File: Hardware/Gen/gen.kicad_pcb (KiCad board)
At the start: 2 copper layers, 149.8 x 76.5 mm, 52 parts, among them J1 Screw_Terminal_01x03, J2 XLR4, J3 XLR3, J4 GAMEN, J5 SHORI, J6 MAE, J7 Screw_Terminal_01x02, J8 PJ-063BH, U1 TPS543021DRLR, U3 TPS560430YDBVR

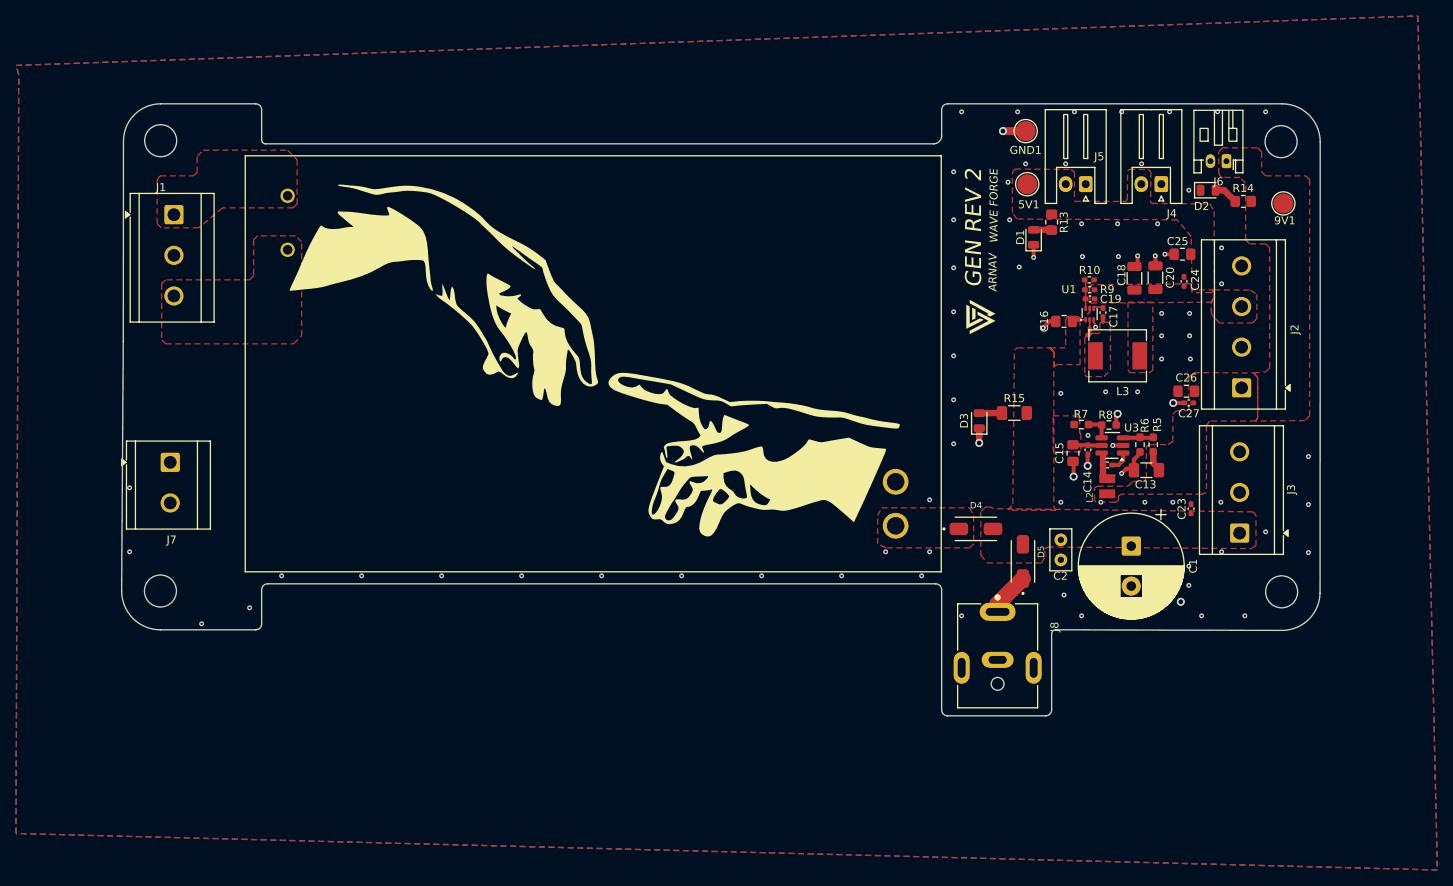
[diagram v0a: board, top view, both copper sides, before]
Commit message: Gen rev 2 Ordered and Assembled. Proven Working All rails Spot on
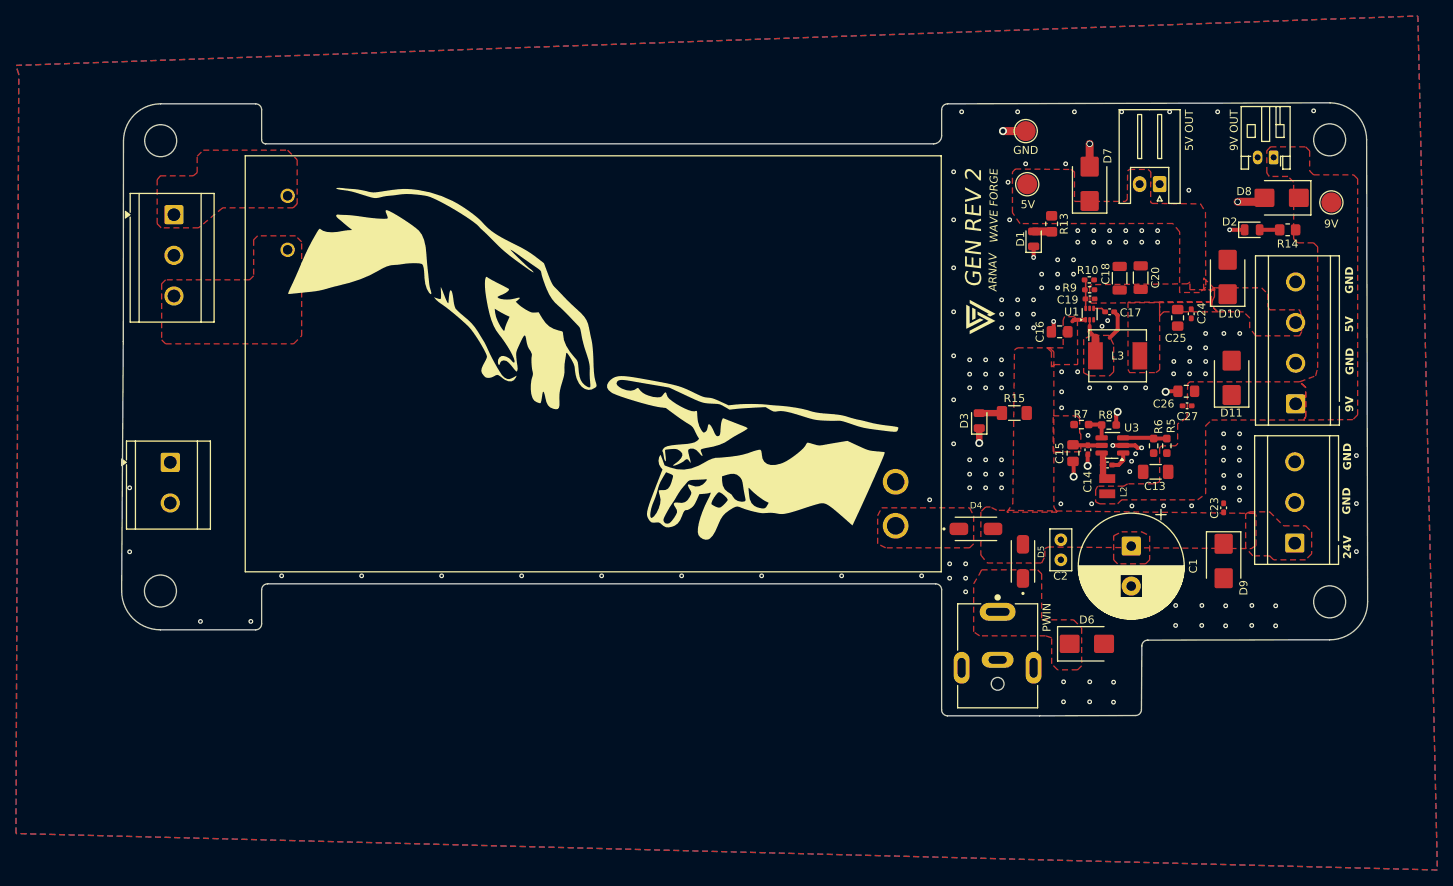
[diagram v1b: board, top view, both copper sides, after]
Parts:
- removed J4: GAMEN, Connector_JST:JST_XH_S2B-XH-A_1x02_P2.50mm_Horizontal
- added D10: SMBJ6.0A, Diode_SMD:D_SMB, F.Cu at (208.2, 102.7)
- added D11: SMBJ6.0A, Diode_SMD:D_SMB, F.Cu at (208.8, 115.2)
- added D6: SMBJ28A, Diode_SMD:D_SMB, F.Cu at (190.7, 148.5)
- added D7: SMBJ6.0A, Diode_SMD:D_SMB, F.Cu at (191.0, 91.0)
- added D8: SMBJ6.0A, Diode_SMD:D_SMB, F.Cu at (215.0, 92.8)
- added D9: SMBJ28A, Diode_SMD:D_SMB, F.Cu at (207.8, 138.2)
- 5V OUT: renamed from J5
- 9V OUT: renamed from J6
- MAINS TO GROUND: renamed from J7
- moved 5V OUT 9.24 mm to (199.8, 91.0)
- moved C25 7.97 mm to (202.0, 107.8), turned to 90 degrees
- moved D2 7.41 mm to (211.3, 96.8)
- moved J2 7.04 mm to (216.8, 118.5)
- moved J3 7.00 mm to (216.6, 135.9)
- moved R14 6.59 mm to (215.8, 96.8)
- moved H3 6.13 mm to (221.0, 143.2)
- moved H3 6.07 mm to (221.0, 85.5)
- moved 9V 6.00 mm to (221.2, 93.3)
- moved 9V OUT 5.92 mm to (214.0, 87.7)
- moved C24 4.15 mm to (203.7, 107.2), turned to 90 degrees
- moved C23 4.07 mm to (207.8, 131.5)
- moved C18 1.85 mm to (194.8, 102.8)
- moved C20 1.85 mm to (197.4, 102.7)
- moved R5 1.71 mm to (200.7, 123.8)
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- renumbered 5V1 to 5V, 9V1 to 9V, GND1 to GND, J8 to PWIN
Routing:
- net Net-(U1-SW): track 2.68 -> 8.64 mm
- net Net-(D5-A): track 5.45 -> 0.00 mm
- net +9V: track 2.38 -> 0.00 mm
- net Net-(U3-FB): track 3.80 -> 5.67 mm
- net GND: track 24.6 -> 25.5 mm, vias 87 -> 157
- net unconnected-(U1-EN-Pad5): track 0.81 -> 0.00 mm
- net Net-(D2-A): track 3.04 -> 2.50 mm
- added copper zone on F.Cu, net Net-(D5-A)
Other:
- board size 149.8 x 76.5 mm -> 155.8 x 76.6 mm
- board text added: "24V"
- board text added: "5V"
- board text added: "9V"
- board text added: "GND"
